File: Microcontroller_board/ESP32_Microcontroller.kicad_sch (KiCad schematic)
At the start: 10 parts, among them SW1 Reset, U1 ESP32-WROOM-E

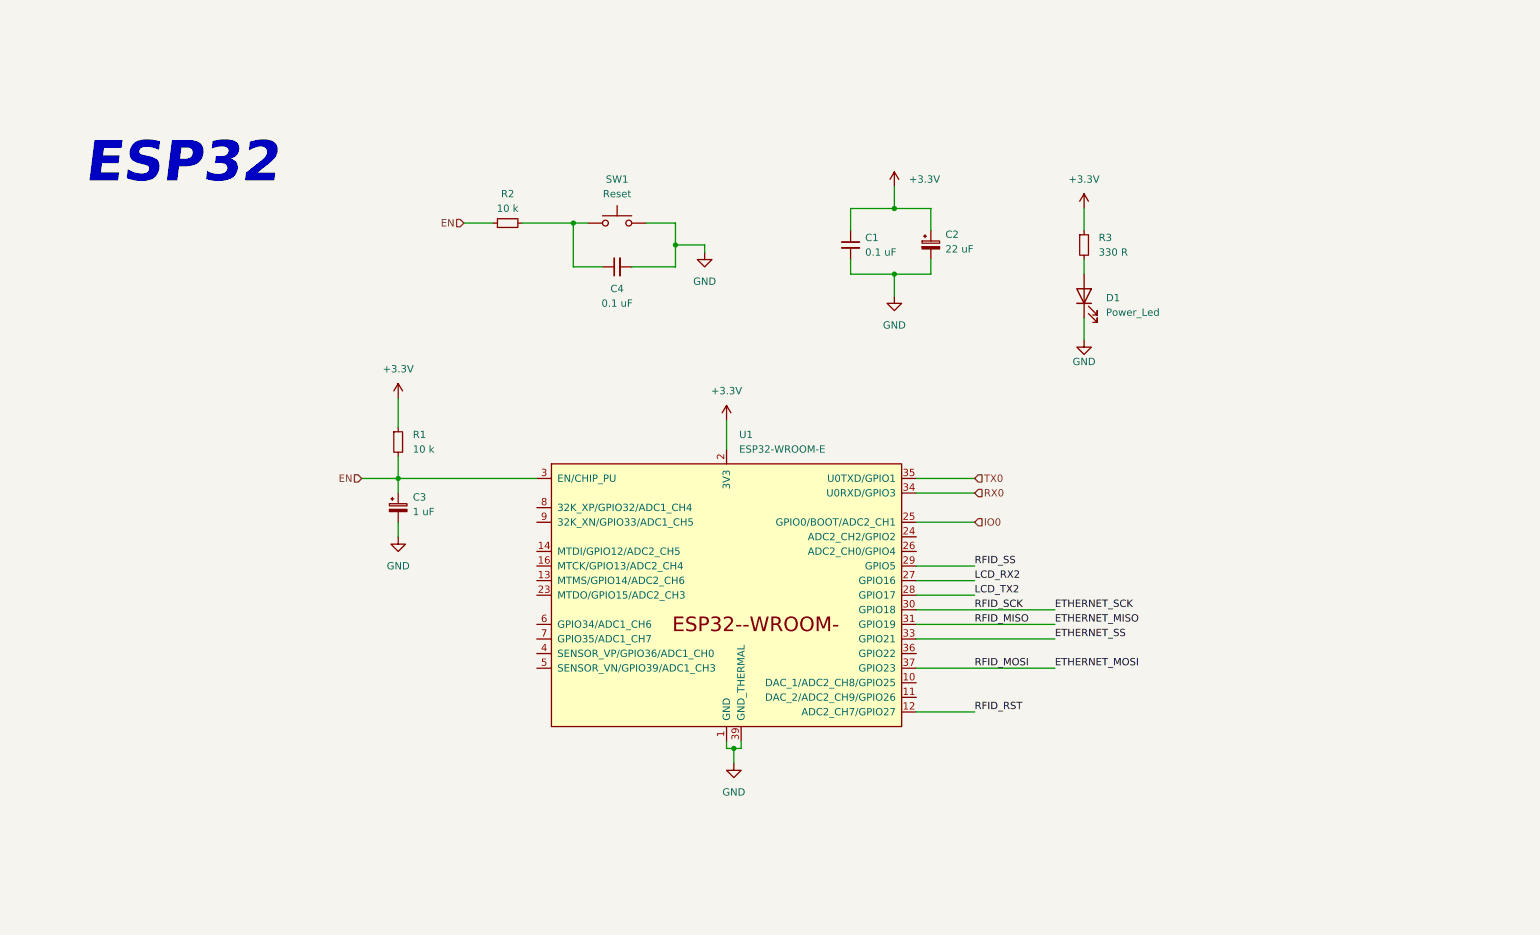
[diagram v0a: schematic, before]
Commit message: Added two more leds and make the schematic a little bit prettier
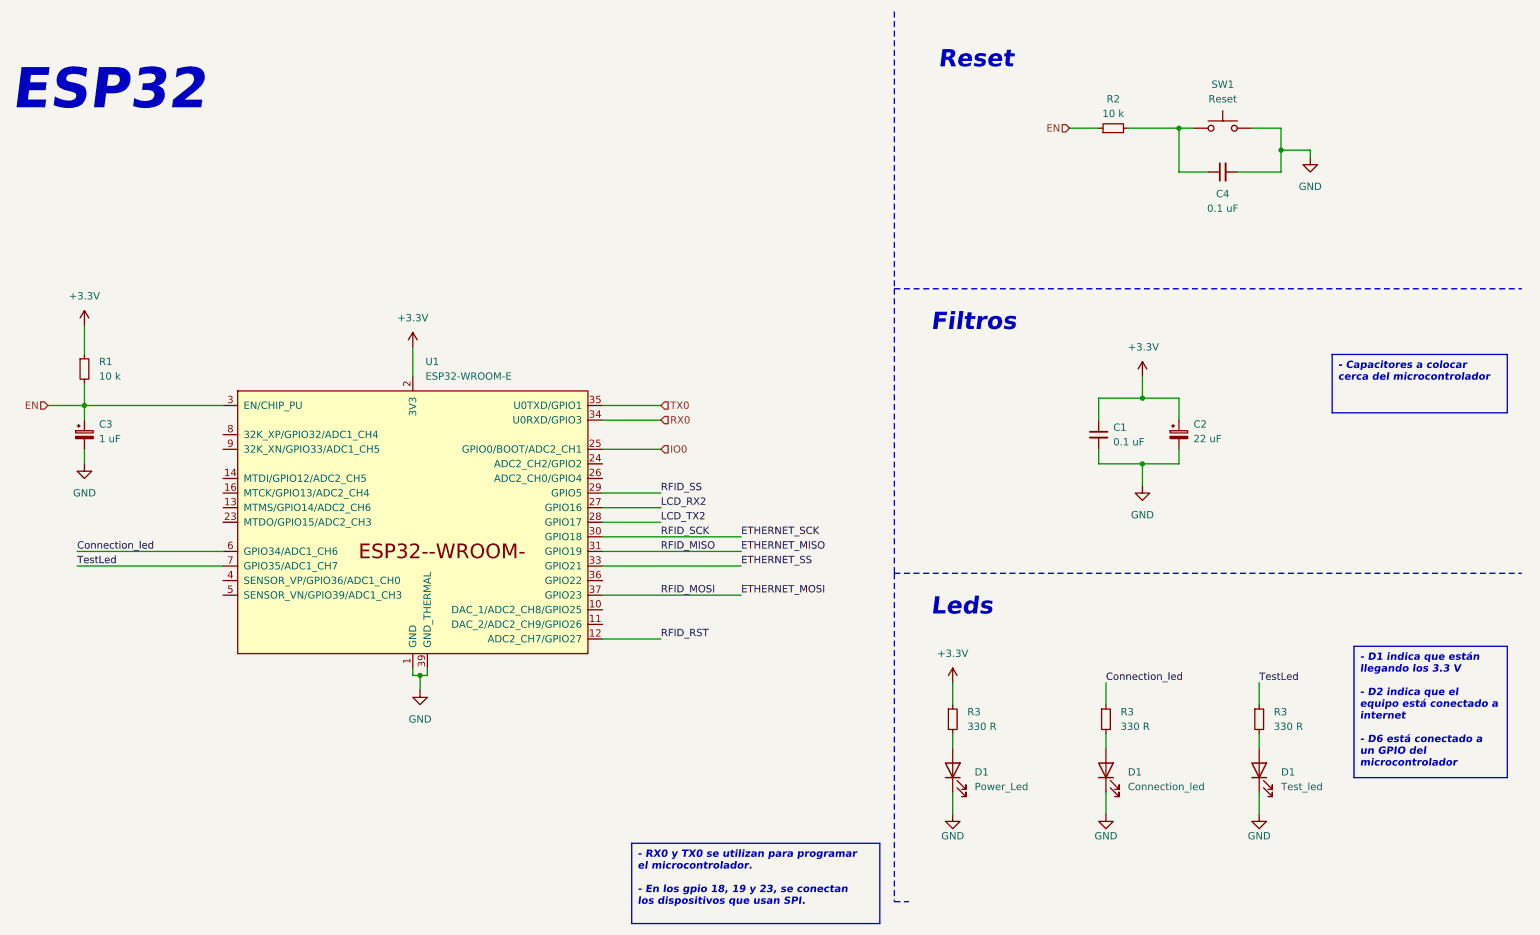
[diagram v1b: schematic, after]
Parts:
- added D1: Connection_led, symbol Device:LED
- added D1: Test_led, symbol Device:LED
- added R3 (x2): 330 R, symbol Device:R_Small
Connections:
- net GND: now also D1.1 (K), D1.1 (K)
- net Connection_led: now reaches U1.6 (GPIO34/ADC1_CH6)
- net Connection_led: now also R3.1
- net TestLed: now reaches U1.7 (GPIO35/ADC1_CH7)
- net TestLed: now also R3.1
- new net: D1.2 (A), R3.2 (x2)
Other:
- note added: "Filtros"
- note added: "Leds"
- note added: "Reset"
- moved on the sheet: C1, C2, C3, C4, D1, R1, R2, R3, SW1, U1

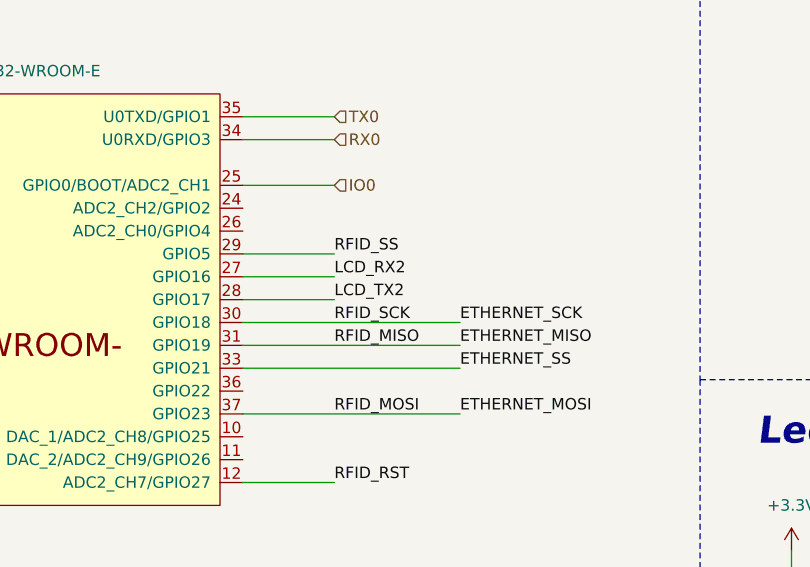
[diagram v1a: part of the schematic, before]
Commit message: Added the connector for LCD Nextion and connected to esp32
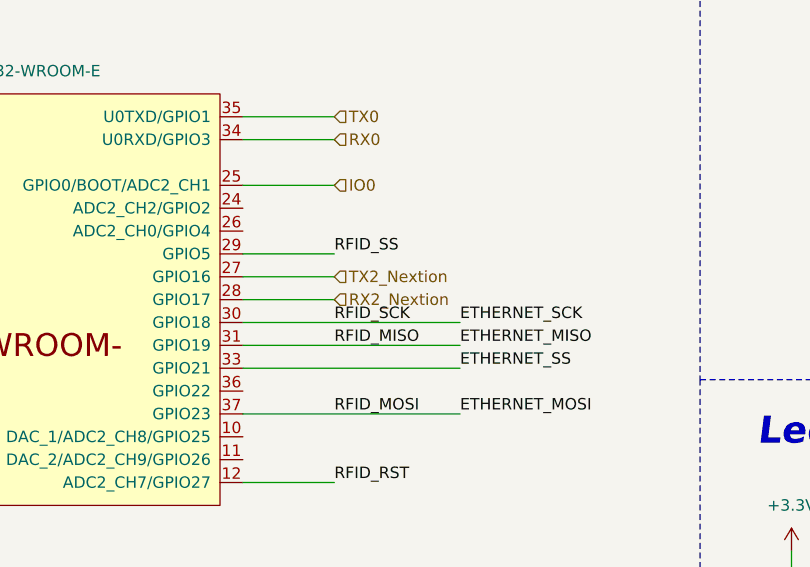
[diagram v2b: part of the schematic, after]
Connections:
- net LCD_RX2 renamed TX2_Nextion
- net LCD_TX2 renamed RX2_Nextion
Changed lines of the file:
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@@
+    (stroke (width 0) (type default))
+  )
+  (polyline (pts (xy 175.26 166.37) (xy 177.8 166.37))
+    (stroke (width 0) (type dash))
+  )
+  (polyline (pts (xy 175.26 11.43) (xy 175.26 59.69))
+    (stroke (width 0) (type dash))
+  )
+  (wire (pts (xy 91.44 127) (xy 92.71 127))
+    (stroke (width 0) (type default))
+  )
+  (wire (pts (xy 218.44 90.17) (xy 224.79 90.17))
+    (stroke (width 0) (type default))
+  )
+  (polyline (pts (xy 175.26 59.69) (xy 284.48 59.69))
+    (stroke (width 0) (type dash))
+  )
+  (wire (pts (xy 124.46 107.95) (xy 148.59 107.95))
+    (stroke (width 0) (type default))
+  )
+  (wire (pts (xy 93.98 127) (xy 93.98 125.73))
+    (stroke (width 0) (type default))
+  )
+  (wire (pts (xy 210.82 90.17) (xy 218.44 90.17))
+    (stroke (width 0) (type default))
+  )
+  (wire (pts (xy 224.79 78.74) (xy 224.79 82.55))
+    (stroke (width 0) (type default))
+  )
+  (wire (pts (xy 124.46 120.65) (xy 134.62 120.65))
+    (stroke (width 0) (type default))
+  )
+  (wire (pts (xy 124.46 102.87) (xy 148.59 102.87))
+    (stroke (width 0) (type default))
+  )
+  (polyline (pts (xy 175.26 59.69) (xy 175.26 109.22))
+    (stroke (width 0) (type dash))
+  )
+  (wire (pts (xy 34.29 76.2) (xy 34.29 80.01))
+    (stroke (width 0) (type default))
+  )
+  (wire (pts (xy 247.65 36.83) (xy 247.65 35.56))
+    (stroke (width 0) (type default))
+  )
+  (wire (pts (xy 247.65 35.56) (xy 242.57 35.56))
+    (stroke (width 0) (type default))
+  )
+  (wire (pts (xy 33.02 107.95) (xy 58.42 107.95))
+    (stroke (width 0) (type default))
+  )
+  (wire (pts (xy 238.76 147.32) (xy 238.76 151.13))
+    (stroke (width 0) (type default))
+  )
+  (wire (pts (xy 212.09 147.32) (xy 212.09 151.13))
+    (stroke (width 0) (type default))
+  )
+  (wire (pts (xy 34.29 87.63) (xy 34.29 90.17))
     (stroke (width 0) (type default))
   )
@@
     (stroke (width 0) (type default))
   )
-  (polyline (pts (xy 175.26 166.37) (xy 177.8 166.37))
-    (stroke (width 0) (type dash))
-  )
-  (polyline (pts (xy 175.26 11.43) (xy 175.26 59.69))
-    (stroke (width 0) (type dash))
-  )
-  (wire (pts (xy 91.44 127) (xy 92.71 127))
-    (stroke (width 0) (type default))
-  )
-  (wire (pts (xy 218.44 90.17) (xy 224.79 90.17))
-    (stroke (width 0) (type default))
-  )
-  (polyline (pts (xy 175.26 59.69) (xy 284.48 59.69))
-    (stroke (width 0) (type dash))
-  )
-  (wire (pts (xy 124.46 107.95) (xy 148.59 107.95))
-    (stroke (width 0) (type default))
-  )
-  (wire (pts (xy 93.98 127) (xy 93.98 125.73))
-    (stroke (width 0) (type default))
-  )
-  (wire (pts (xy 210.82 90.17) (xy 218.44 90.17))
-    (stroke (width 0) (type default))
-  )
-  (wire (pts (xy 224.79 78.74) (xy 224.79 82.55))
-    (stroke (width 0) (type default))
-  )
-  (wire (pts (xy 124.46 120.65) (xy 134.62 120.65))
-    (stroke (width 0) (type default))
-  )
-  (wire (pts (xy 124.46 102.87) (xy 148.59 102.87))
-    (stroke (width 0) (type default))
-  )
-  (polyline (pts (xy 175.26 59.69) (xy 175.26 109.22))
-    (stroke (width 0) (type dash))
-  )
-  (wire (pts (xy 34.29 76.2) (xy 34.29 80.01))
-    (stroke (width 0) (type default))
-  )
-  (wire (pts (xy 247.65 36.83) (xy 247.65 35.56))
-    (stroke (width 0) (type default))
-  )
-  (wire (pts (xy 247.65 35.56) (xy 242.57 35.56))
-    (stroke (width 0) (type default))
-  )
-  (wire (pts (xy 33.02 107.95) (xy 58.42 107.95))
-    (stroke (width 0) (type default))
-  )
-  (wire (pts (xy 238.76 147.32) (xy 238.76 151.13))
-    (stroke (width 0) (type default))
-  )
-  (wire (pts (xy 212.09 147.32) (xy 212.09 151.13))
-    (stroke (width 0) (type default))
-  )
-  (wire (pts (xy 34.29 87.63) (xy 34.29 90.17))
-    (stroke (width 0) (type default))
-  )
   (wire (pts (xy 124.46 87.63) (xy 134.62 87.63))
     (stroke (width 0) (type default))
@@
     (stroke (width 0) (type default))
   )
+  (wire (pts (xy 124.46 97.79) (xy 134.62 97.79))
+    (stroke (width 0) (type default))
+  )
   (wire (pts (xy 224.79 39.37) (xy 224.79 31.75))
-    (stroke (width 0) (type default))
-  )
-  (wire (pts (xy 124.46 97.79) (xy 134.62 97.79))
     (stroke (width 0) (type default))
   )
@@
     (effects (font (size 1.27 1.27)) (justify left bottom))
   )
-  (label "LCD_TX2" (at 134.62 100.33 0) (fields_autoplaced)
-    (effects (font (size 1.27 1.27)) (justify left bottom))
-  )
   (label "ETHERNET_SS" (at 148.59 107.95 0) (fields_autoplaced)
     (effects (font (size 1.27 1.27)) (justify left bottom))
@@
   )
   (label "Connection_led" (at 33.02 105.41 0) (fields_autoplaced)
-    (effects (font (size 1.27 1.27)) (justify left bottom))
-  )
-  (label "LCD_RX2" (at 134.62 97.79 0) (fields_autoplaced)
     (effects (font (size 1.27 1.27)) (justify left bottom))
   )
@@
     (effects (font (size 1.27 1.27)) (justify right))
   )
+  (hierarchical_label "TX2_Nextion" (shape input) (at 134.62 97.79 0) (fields_autoplaced)
+    (effects (font (size 1.27 1.27)) (justify left))
+  )
   (hierarchical_label "RX0" (shape input) (at 134.62 82.55 0) (fields_autoplaced)
     (effects (font (size 1.27 1.27)) (justify left))
@@
     (effects (font (size 1.27 1.27)) (justify left))
   )
+  (hierarchical_label "RX2_Nextion" (shape input) (at 134.62 100.33 0) (fields_autoplaced)
+    (effects (font (size 1.27 1.27)) (justify left))
+  )
